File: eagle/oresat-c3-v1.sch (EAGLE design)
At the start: 112 parts, among them J1 J-SAMTEC-TFM-110-X1-XXX-D-RA, J10 2X8X1.27, J11 2X8X1.27, J12 2X8X1.27, J2 U.FL, J3 U.FL, J4 U.FL, J6 J-SAMTEC-TFM-120-X1-XXX-D-RA, J7 FTSH-105-XX-X-DV-K, J9 2X8X1.27, U1 MAX892LEUA+T21-0036K-L, U2 TCAN330, U3 TCAN330, U4 TPS259621 - eFuse, U5 TPS62111RSA, U6 MAX6374KA-T21-0078H-L, U7 STM32F446RE, X1 16MHZ-2.5x2mm

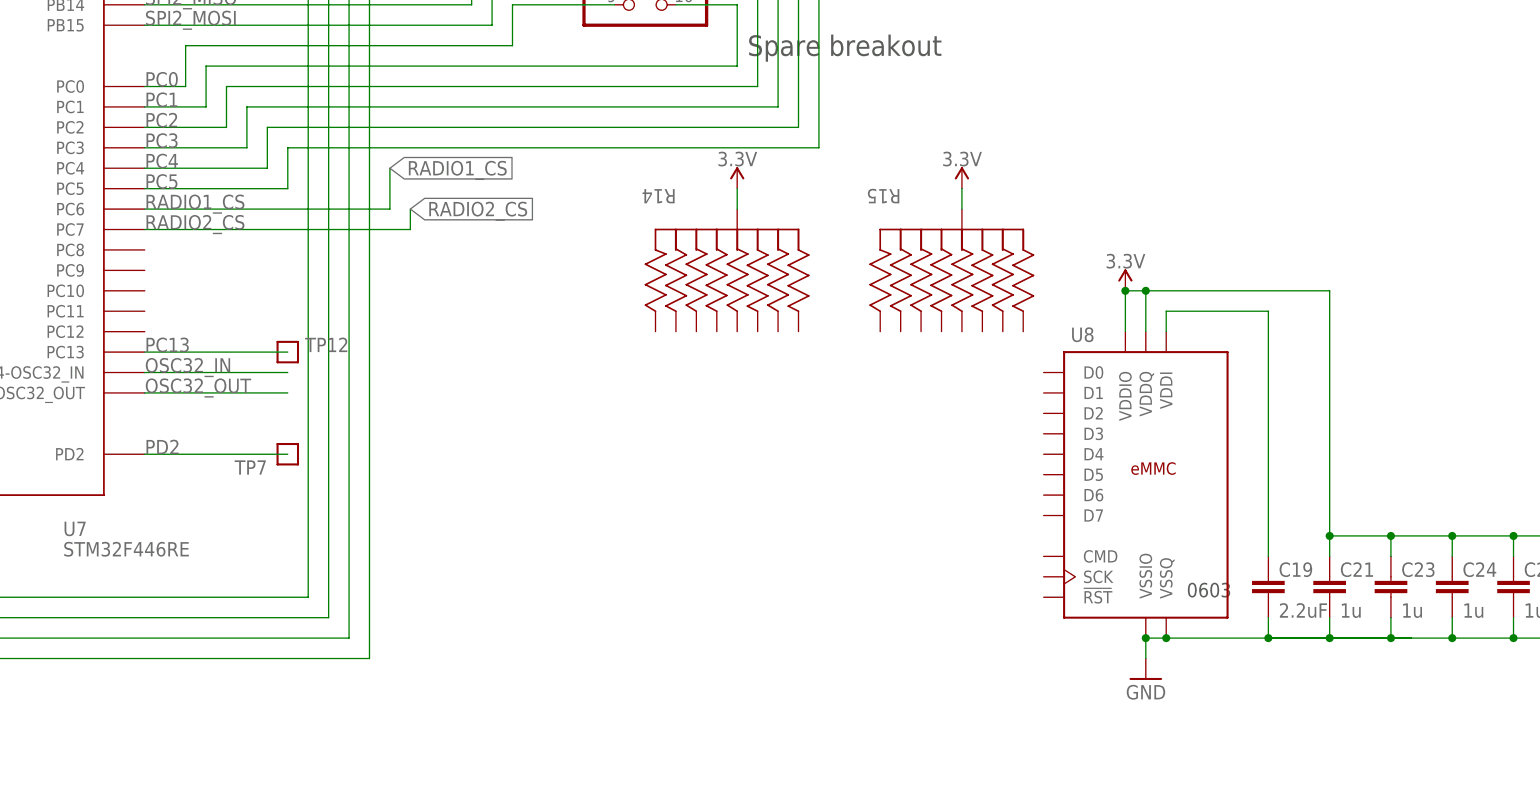
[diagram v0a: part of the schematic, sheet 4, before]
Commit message: Added eMMC
Almost completed adding eMMC
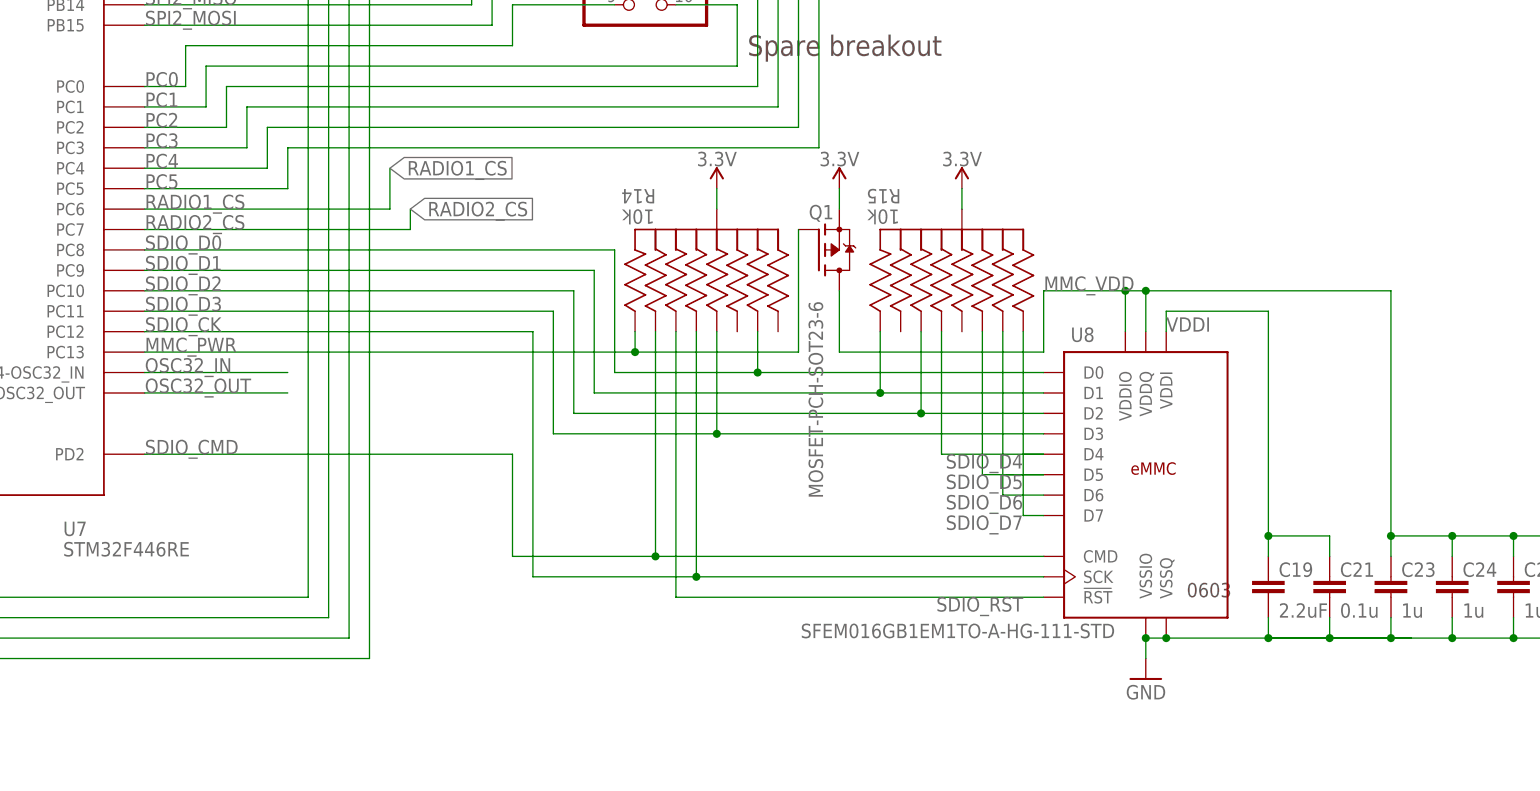
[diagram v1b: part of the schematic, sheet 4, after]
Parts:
- removed TP12, TP7: TEST-POINT, Tova:TEST-POINT
- added Q1: MOSFET-PCH-SOT23-6, Q-MOSFET-PCH-SOT23-6:MOSFET-PCH-SOT23-6
- C21: value 1u -> 0.1u
- R14, R15: value (none) -> 10k
- U8: value (none) -> SFEM016GB1EM1TO-A-HG-111-STD
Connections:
- removed net N$6: C19.1, U8.VDDI
- removed net PC13: TP12.1, U7.PC13
- removed net PD2: TP7.1, U7.PD2
- new net MMC_PWR: Q1.G, R14.11, U7.PC13
- new net MMC_VDD: C23.1, C24.1, C25.1, C26.1, Q1.D, U8.VDDIO, U8.VDDQ
- new net SDIO_CK: R14.88, U7.PC12, U8.SCK
- new net SDIO_CMD: R14.99, U7.PD2, U8.CMD
- new net SDIO_D0: R14.44, U7.PC8, U8.D0
- new net SDIO_D1: R15.11, U7.PC9, U8.D1
- new net SDIO_D2: R15.22, U7.PC10, U8.D2
- new net SDIO_D3: R14.33, U7.PC11, U8.D3
- new net SDIO_D4: R15.88, U8.D4
- new net SDIO_D5: R15.77, U8.D5
- new net SDIO_D6: R15.44, U8.D6
- new net SDIO_D7: R15.66, U8.D7
- new net SDIO_RST: R14.22, U8.!RST!
- new net VDDI: C19.1, C21.1, U8.VDDI
- net 3.3V: now also Q1.S; no longer C21.1, C23.1, C24.1, C25.1, C26.1, U8.VDDIO, U8.VDDQ
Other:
- moved on the sheet: C4, R14

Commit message: integrated 2 AX5043 radios and connected up the eMMC
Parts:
- removed J10, J11, J9: 2X8X1.27, 2x8x1.27:2X8X1.27
- removed JP3: (no value), pinhead:PINHD-1X3
- removed JP5: (no value), pinhead:PINHD-1X5
- removed TP21, TP9: TEST-POINT, Tova:TEST-POINT
- added C42, C43, C58, C59: 8.2p, oresat-rcl:C-EU0402-C-NOSILK
- added C44, C45, C60, C61: 1n, oresat-rcl:C-EU0402-C-NOSILK
- added C46, C47, C62, C63: 82p, oresat-rcl:C-EU0402-C-NOSILK
- added C48, C49, C64, C65: 22p, oresat-rcl:C-EU0402-C-NOSILK
- added C50, C53, C66, C69: 22n, oresat-rcl:C-EU0603-C-NOSILK
- added C51, C54, C67, C70: NP, oresat-rcl:C-EU0603-C-NOSILK
- added C52, C55, C68, C71: 4.7u, oresat-rcl:C-EU0603-C-NOSILK
- added C56, C72: 10n, oresat-rcl:C-EU0603-C-NOSILK
- added C57, C73: 1u, oresat-rcl:C-EU0603-C-NOSILK
- added D8, D9: GREEN, SparkFun-LED:LED-GREEN0603
- added J13, J14, J16, J17, J18: U.FL, SparkFun-Connectors:U.FL
- added J15, J19: HARWIN-2X8X1.27, J-Harwin-M50-3610842R-2X8X1.27_Male :HARWIN-2X8X1.27
- added JP4, JP6: (no value), J-2X8X1.27:PINHD-1X2
- added L10, L11, L6, L7: 43n, oresat-rcl:L-US0402-C-NOSILK
- added L12, L13, L8, L9: 91n, oresat-rcl:L-US0603-C-NOSILK
- added R28, R34: 150, oresat-rcl:R-US_0402-C-NOSILK
- added R29, R35: 0, oresat-rcl:R-US_0402-C-NOSILK
- added R30, R37: NP, oresat-rcl:R-US_0402-C-NOSILK
- added R31, R38: 1.5k, oresat-rcl:R-US_0603-B-NOSILK
- added R32, R33, R39, R40: 0, oresat-rcl:R-US_0603-C-NOSILK
- added U11, U13: U-ONSEMI-AX5043, U-ON-Semi-AX5043-radio:U-ONSEMI-AX5043
- added U12, U14: LP2985XX-N, U-TI-LP2985XX-N-linear-reg:LP2985XX-N
- added X3, X4: TAITIEN-TY, X-Taitien-TY-TCXO:TAITIEN-TY
- D3: value RED -> GREEN
- D4: value AMBER -> GREEN
- J12: value 2X8X1.27 -> U.FL; device 2x8x1.27:2X8X1.27 -> SparkFun-Connectors:U.FL
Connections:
- removed net RADIO1_SYSCLK: J12.3, TP21.1
- removed net RADIO2_SYSCLK: J10.3, TP9.1
- new net 1V1: C50.1, C51.1, C52.1, U12.VOUT, X3.VDD
- new net 1V2: C66.1, C67.1, C68.1, U14.VOUT, X4.VDD
- new net ANTN1: C42.2, L7.2, U11.ANTN
- new net ANTN2: C58.2, L11.2, U13.ANTN
- new net ANTP2: C43.2, L6.2, L8.1, U11.ANTP
- new net ANTP3: C49.2, L9.2, U11.ANTP1
- new net ANTP4: C59.2, L10.2, L12.1, U13.ANTP
- new net ANTP5: C65.2, L13.2, U13.ANTP1
- new net CLKN1: C44.1, R28.1, U11.CLK16N
- new net CLKN2: C60.1, R34.1, U13.CLK16N
- new net CLKP1: C45.1, R28.2, U11.CLK16P
- new net CLKP2: C61.1, R34.2, U13.CLK16P
- new net CS1: J15.1, U11.CS
- new net CS2: J19.1, U13.CS
- new net GNDR: C43.1, C44.2, C46.2, C47.1, C50.2, C51.2, C52.2, C53.2, C54.2, C55.2, C56.2, C57.2, C59.1, C60.2, C62.2, C63.1, C66.2, C67.2, C68.2, C69.2, C70.2, C71.2, C72.2, C73.2, D8.C, D9.C, J15.15, J19.15, L11.1, L12.2, L13.1, L7.1, L8.2, L9.1, R30.2, R37.2, U11.GND1, U11.GND2, U11.PGND, U12.GND, U13.GND1, U13.GND2, U13.PGND, U14.GND, X3.GND, X4.GND
- new net IRQ1: J15.9, U11.IRQ
- new net IRQ2: J19.9, U13.IRQ
- new net LEDPWR1: D8.A, R31.2
- new net LEDPWR2: D9.A, R38.2
- new net MISO1: J15.5, U11.MISO
- new net MISO2: J19.5, U13.MISO
- new net MOSI1: J15.7, U11.MOSI
- new net MOSI2: J19.7, U13.MOSI
- new net N$10: C56.1, U12.BYPASS
- new net N$11: C42.1, C48.2, L6.1
- new net N$12: C45.2, X3.OUT
- new net N$13: U13.L1, U13.L2
- new net N$14: C62.1, U13.VDD_A1
- new net N$15: C63.2, U13.VDD_A2
- new net N$16: C72.1, U14.BYPASS
- new net N$17: C58.1, C64.2, L10.1
- new net N$18: C61.2, X4.OUT
- new net N$7: U11.L1, U11.L2
- new net N$8: C46.1, U11.VDD_A1
- new net N$9: C47.2, U11.VDD_A2
- new net PWRAMP1: J15.11, U11.PWRAMP
- new net PWRAMP2: J19.11, U13.PWRAMP
- new net RADIO1_PTT: J15.12
- new net RADIO2_PTT: J19.12
- new net REF-OUT1: J14.SIGNAL, R29.2, R30.1
- new net REF-OUT2: J18.SIGNAL, R35.2, R37.1
- new net RX1: C48.1, J12.SIGNAL
- new net RX2: C64.1, J16.SIGNAL
- new net SCLK1: J15.3, U11.SCLK
- new net SCLK2: J19.3, U13.SCLK
- new net SYSCLK1: R29.1, U11.SYSCLK
- new net SYSCLK2: R35.1, U13.SYSCLK
- new net TX1: C49.1, J13.SIGNAL
- new net TX2: C65.1, J17.SIGNAL
- net 3.3V: now also C53.1, C54.1, C55.1, C57.1, C69.1, C70.1, C71.1, C73.1, JP6.1, JP6.2, R31.1, R32.1, R32.2, R33.1, R33.2, R38.1, R39.1, R39.2, R40.1, R40.2, U11.VDD_IO, U12.EN, U12.VIN, U13.VDD_IO, U14.EN, U14.VIN; no longer J11.13, J11.3, J9.13, J9.3, JP5.1, JP5.2, JP5.3, JP5.4, JP5.5
- net GND: no longer J10.1, J10.10, J10.12, J10.14, J10.15, J10.16, J10.2, J10.4, J10.6, J10.8, J11.1, J11.10, J11.12, J11.14, J11.15, J11.16, J11.2, J11.4, J11.6, J11.8, J12.1, J12.10, J12.12, J12.14, J12.15, J12.16, J12.2, J12.4, J12.6, J12.8, J9.1, J9.10, J9.12, J9.14, J9.15, J9.16, J9.2, J9.4, J9.6, J9.8
- net RADIO1_CS: now also J15.2; no longer J12.5
- net RADIO1_IRQ: now also J15.10; no longer J12.13
- net RADIO2_CS: now also J19.2; no longer J10.5
- net RADIO2_IRQ: now also J19.10; no longer J10.13
- net SPI1_MISO: now also J15.6, J19.6; no longer J10.9, J12.9
- net SPI1_MOSI: now also J15.8, J19.8; no longer J10.11, J12.11
- net SPI1_SCK: now also J15.4, J19.4; no longer J10.7, J12.7
- net VBUSP: now also JP4.1, JP4.2; no longer JP3.1, JP3.2, JP3.3
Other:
- note added: "1.8V LDO"
- note added: "ADCs"
- note added: "AX5043 Radios"
- note added: "Control"
- note added: "Device Operating Range: 400 - 525 MHz 800 - 1050 MHz"
- note added: "PWR"
- note added: "Ref-Out"
- note added: "Rx"
- note added: "SPI / IRQ"
- note added: "Tx"

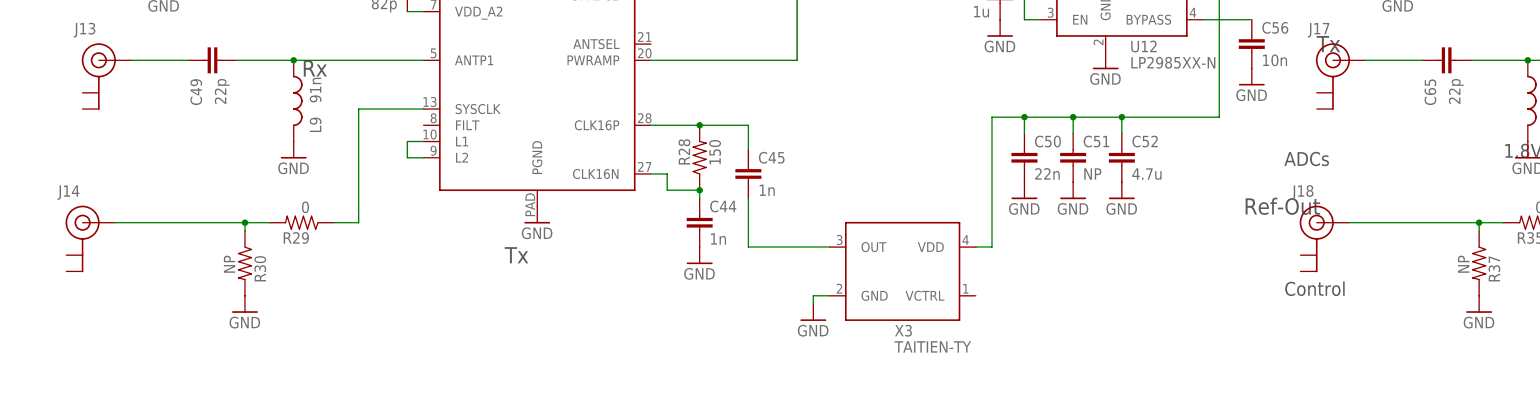
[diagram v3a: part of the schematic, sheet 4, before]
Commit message: Ran an initial ERC DRC on the v1 board, cleared some errors and left the rest for a board review
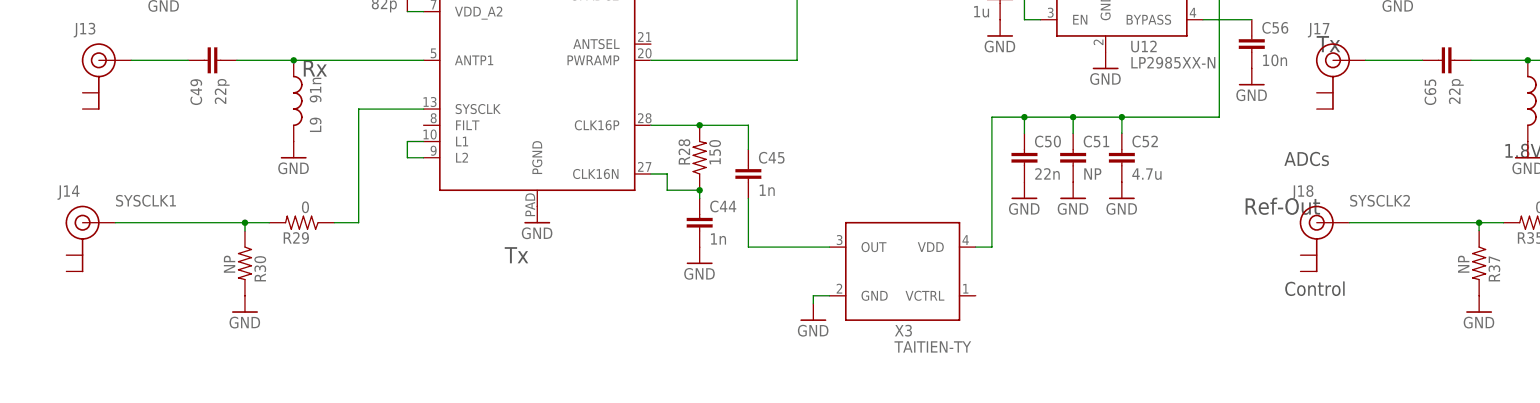
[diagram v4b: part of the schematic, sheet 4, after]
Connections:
- removed net REF-OUT1: J14.SIGNAL, R29.2, R30.1
- removed net REF-OUT2: J18.SIGNAL, R35.2, R37.1
- net SYSCLK1: now also J14.SIGNAL, R29.2, R30.1
- net SYSCLK2: now also J18.SIGNAL, R35.2, R37.1
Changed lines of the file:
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@@
 <?xml version="1.0" encoding="utf-8"?>
 <!DOCTYPE eagle SYSTEM "eagle.dtd">
-<eagle version="9.5.2">
+<eagle version="9.5.1">
 <drawing>
 <settings>
@@
 <wire x1="88.9" y1="149.86" x2="85.09" y2="149.86" width="0.1524" layer="91"/>
 </segment>
+<segment>
+<pinref part="R29" gate="R" pin="2"/>
+<wire x1="50.8" y1="149.86" x2="71.12" y2="149.86" width="0.1524" layer="91"/>
+<pinref part="R30" gate="R" pin="1"/>
+<wire x1="71.12" y1="149.86" x2="74.93" y2="149.86" width="0.1524" layer="91"/>
+<wire x1="71.12" y1="148.59" x2="71.12" y2="149.86" width="0.1524" layer="91"/>
+<junction x="71.12" y="149.86"/>
+<pinref part="J14" gate="G$1" pin="SIGNAL"/>
+<label x="50.8" y="152.4" size="1.778" layer="95"/>
+</segment>
 </net>
 <net name="IRQ1" class="0">
@@
 </segment>
 </net>
-<net name="REF-OUT1" class="1">
-<segment>
-<pinref part="R29" gate="R" pin="2"/>
-<wire x1="50.8" y1="149.86" x2="71.12" y2="149.86" width="0.1524" layer="91"/>
-<pinref part="R30" gate="R" pin="1"/>
-<wire x1="71.12" y1="149.86" x2="74.93" y2="149.86" width="0.1524" layer="91"/>
-<wire x1="71.12" y1="148.59" x2="71.12" y2="149.86" width="0.1524" layer="91"/>
-<junction x="71.12" y="149.86"/>
-<pinref part="J14" gate="G$1" pin="SIGNAL"/>
-</segment>
-</net>
 <net name="1V1" class="0">
 <segment>
@@
 <wire x1="281.94" y1="149.86" x2="278.13" y2="149.86" width="0.1524" layer="91"/>
 </segment>
+<segment>
+<pinref part="R35" gate="R" pin="2"/>
+<wire x1="243.84" y1="149.86" x2="264.16" y2="149.86" width="0.1524" layer="91"/>
+<pinref part="R37" gate="R" pin="1"/>
+<wire x1="264.16" y1="149.86" x2="267.97" y2="149.86" width="0.1524" layer="91"/>
+<wire x1="264.16" y1="148.59" x2="264.16" y2="149.86" width="0.1524" layer="91"/>
+<junction x="264.16" y="149.86"/>
+<pinref part="J18" gate="G$1" pin="SIGNAL"/>
+<label x="243.84" y="152.4" size="1.778" layer="95"/>
+</segment>
 </net>
 <net name="IRQ2" class="0">
@@
 </segment>
 </net>
-<net name="REF-OUT2" class="1">
-<segment>
-<pinref part="R35" gate="R" pin="2"/>
-<wire x1="243.84" y1="149.86" x2="264.16" y2="149.86" width="0.1524" layer="91"/>
-<pinref part="R37" gate="R" pin="1"/>
-<wire x1="264.16" y1="149.86" x2="267.97" y2="149.86" width="0.1524" layer="91"/>
-<wire x1="264.16" y1="148.59" x2="264.16" y2="149.86" width="0.1524" layer="91"/>
-<junction x="264.16" y="149.86"/>
-<pinref part="J18" gate="G$1" pin="SIGNAL"/>
-</segment>
-</net>

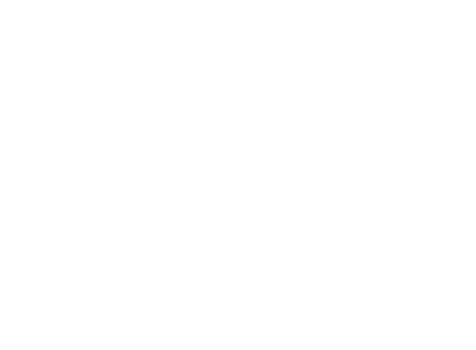
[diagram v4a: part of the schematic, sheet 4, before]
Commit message: implemented changes after design Review with Andrew
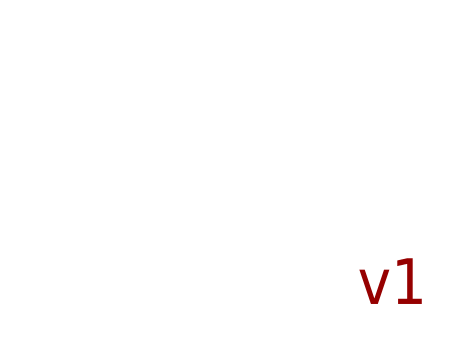
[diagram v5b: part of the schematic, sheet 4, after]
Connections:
- removed net GNDR: C43.1, C44.2, C46.2, C47.1, C50.2, C51.2, C52.2, C53.2, C54.2, C55.2, C56.2, C57.2, C59.1, C60.2, C62.2, C63.1, C66.2, C67.2, C68.2, C69.2, C70.2, C71.2, C72.2, C73.2, D8.C, D9.C, J15.15, J19.15, L11.1, L12.2, L13.1, L7.1, L8.2, L9.1, R30.2, R37.2, U11.GND1, U11.GND2, U11.PGND, U12.GND, U13.GND1, U13.GND2, U13.PGND, U14.GND, X3.GND, X4.GND
- net GND: now also C43.1, C44.2, C46.2, C47.1, C50.2, C51.2, C52.2, C53.2, C54.2, C55.2, C56.2, C57.2, C59.1, C60.2, C62.2, C63.1, C66.2, C67.2, C68.2, C69.2, C70.2, C71.2, C72.2, C73.2, D8.C, D9.C, J15.15, J19.15, L11.1, L12.2, L13.1, L7.1, L8.2, L9.1, R30.2, R37.2, U11.GND1, U11.GND2, U11.PGND, U12.GND, U13.GND1, U13.GND2, U13.PGND, U14.GND, X3.GND, X4.GND
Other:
- note added: "v1"
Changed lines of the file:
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@@
 400 - 525 MHz
 800 - 1050 MHz</text>
+<text x="417.576" y="6.604" size="5.08" layer="94">v1</text>
 </plain>
 <instances>
@@
 </busses>
 <nets>
-<net name="GNDR" class="0">
+<net name="GND" class="0">
 <segment>
 <pinref part="U11" gate="G$1" pin="PGND"/>

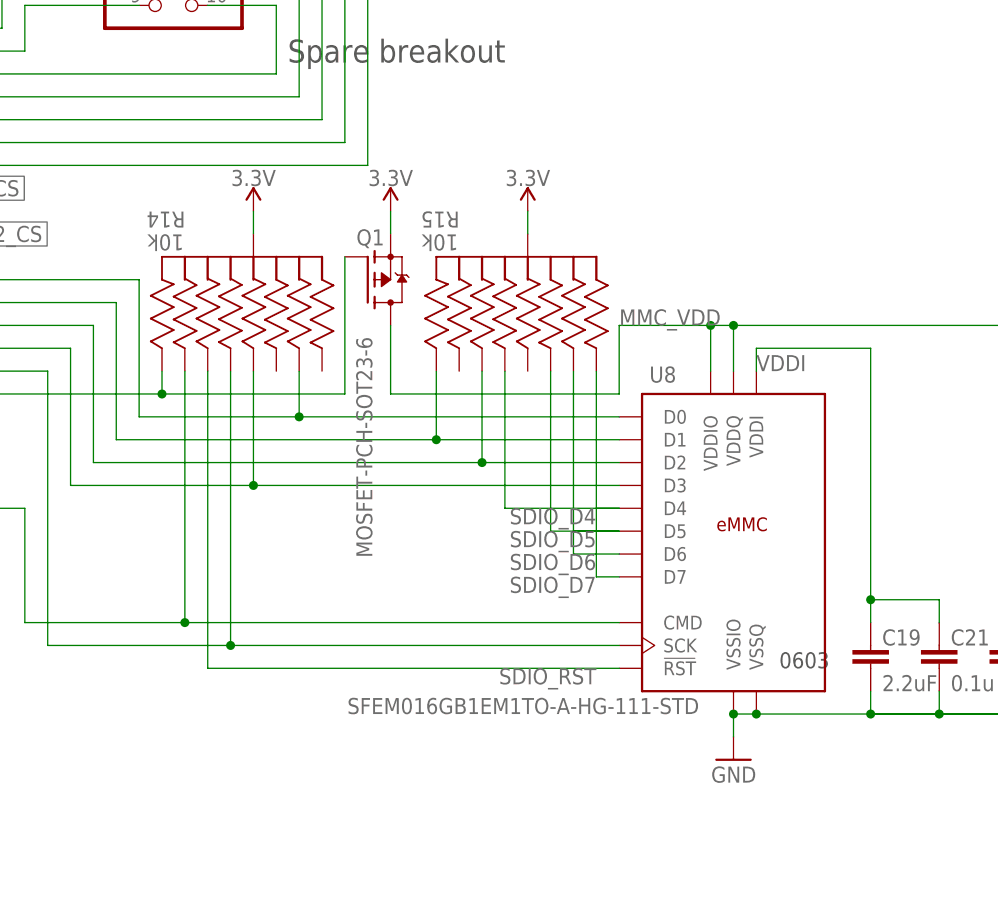
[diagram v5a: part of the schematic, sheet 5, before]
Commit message: Cleared errors for eMMC Added documentation for eMMC
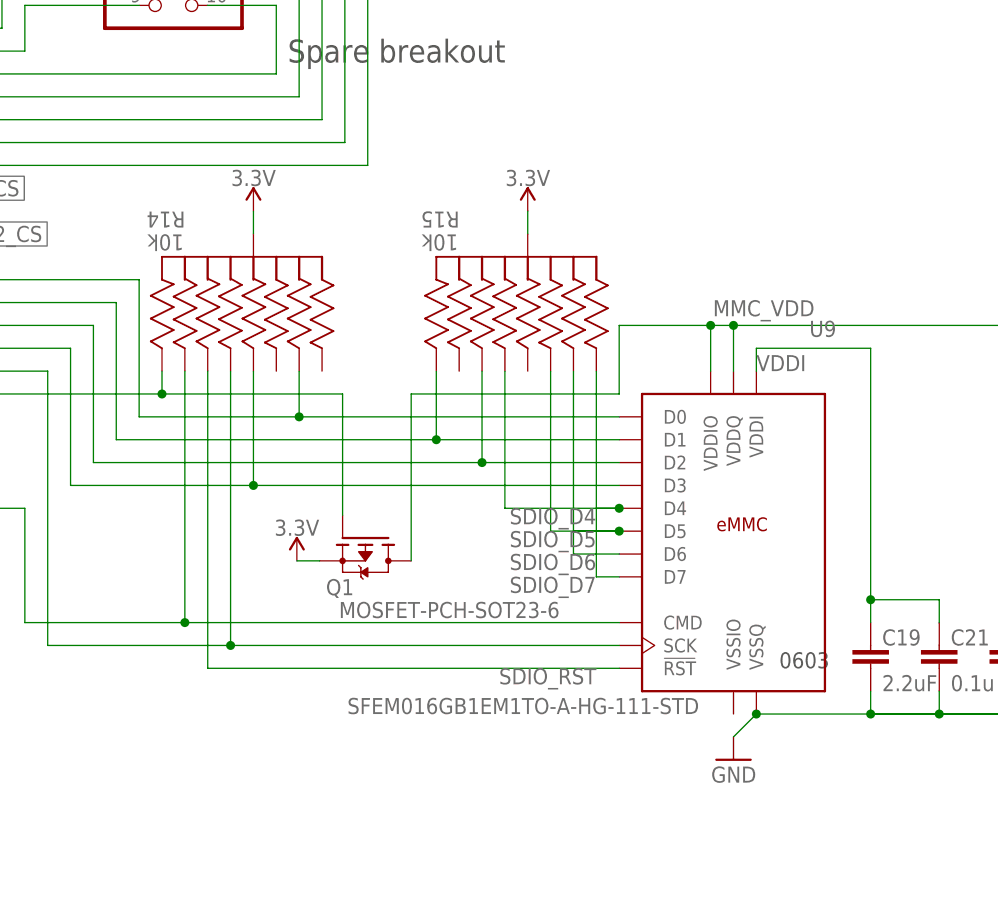
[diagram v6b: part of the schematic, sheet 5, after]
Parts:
- removed U8: SFEM016GB1EM1TO-A-HG-111-STD, U-Generic-eMMC-153pin:EMMC+RESET-BA
- added U9: SFEM016GB1EM1TO-A-HG-111-STD, U-C3-eMMC-153pin:EMMC+RESET-BA
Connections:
- net GND: now also U9.VSSIO, U9.VSSQ; no longer U8.VSSIO, U8.VSSQ
- net MMC_VDD: now also U9.VDDIO, U9.VDDQ; no longer U8.VDDIO, U8.VDDQ
- net SDIO_CK: now also U9.SCK; no longer U8.SCK
- net SDIO_CMD: now also U9.CMD; no longer U8.CMD
- net SDIO_D0: now also U9.D0; no longer U8.D0
- net SDIO_D1: now also U9.D1; no longer U8.D1
- net SDIO_D2: now also U9.D2; no longer U8.D2
- net SDIO_D3: now also U9.D3; no longer U8.D3
- net SDIO_D4: now also U9.D4; no longer U8.D4
- net SDIO_D5: now also U9.D5; no longer U8.D5
- net SDIO_D6: now also U9.D6; no longer U8.D6
- net SDIO_D7: now also U9.D7; no longer U8.D7
- net SDIO_RST: now also U9.!RST!; no longer U8.!RST!
- net VDDI: now also U9.VDDI; no longer U8.VDDI
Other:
- moved on the sheet: Q1
